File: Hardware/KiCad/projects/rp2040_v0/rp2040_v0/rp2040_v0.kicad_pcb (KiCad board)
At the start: 2 copper layers, 142 parts, among them J1 Conn_01x03, J11 Conn_01x02, J12 Screw_Terminal_01x02, J13 Conn_02x09_Counter_Clockwise, J14 Conn_02x06_Odd_Even, J15 Conn_01x02, J17 Conn_01x03, J18 Conn_01x03, J19 Conn_01x03, J2 Conn_01x02, J20 Conn_01x03, J21 Conn_01x03, J22 Conn_02x05_Odd_Even, J23 Screw_Terminal_01x02, J25 Screw_Terminal_01x02, J27 Screw_Terminal_01x02, J28 Screw_Terminal_01x02, J3 Conn_01x03, J4 Conn_01x04, J5 USB_B_Micro, J8 Conn_01x03, J9 Conn_01x02, Q1 2N7002, Q2 AO3400A, Q3 2N7002, Q4 AO3400A, Q5 AO3400A, U1 W25Q128JVSIQTR, U11 AMS1117-5.0, U12 DRV8837, U2 AMS1117-3.3, U3 RP2040, U4 AMS1117-5.0, U5 BMI088, U6 BMP280, U7 AMS1117-5.0, U8 AMS1117-5.0, U9 AMS1117-5.0, X1 X322512MSB4SI (12MHz)

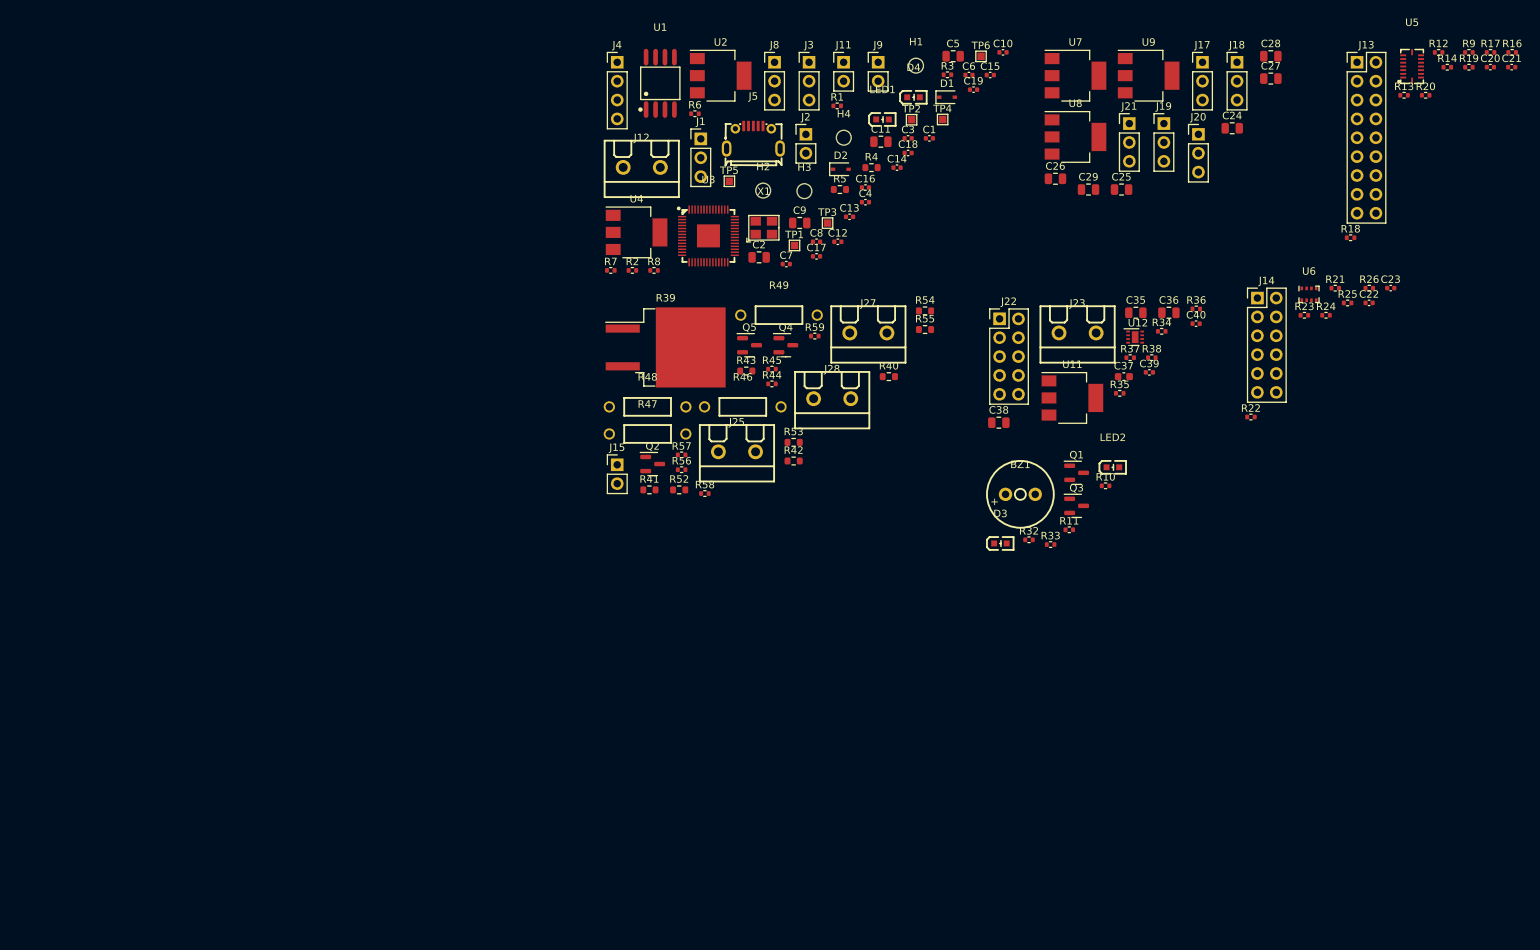
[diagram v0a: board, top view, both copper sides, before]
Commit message: Update leds and further layout work
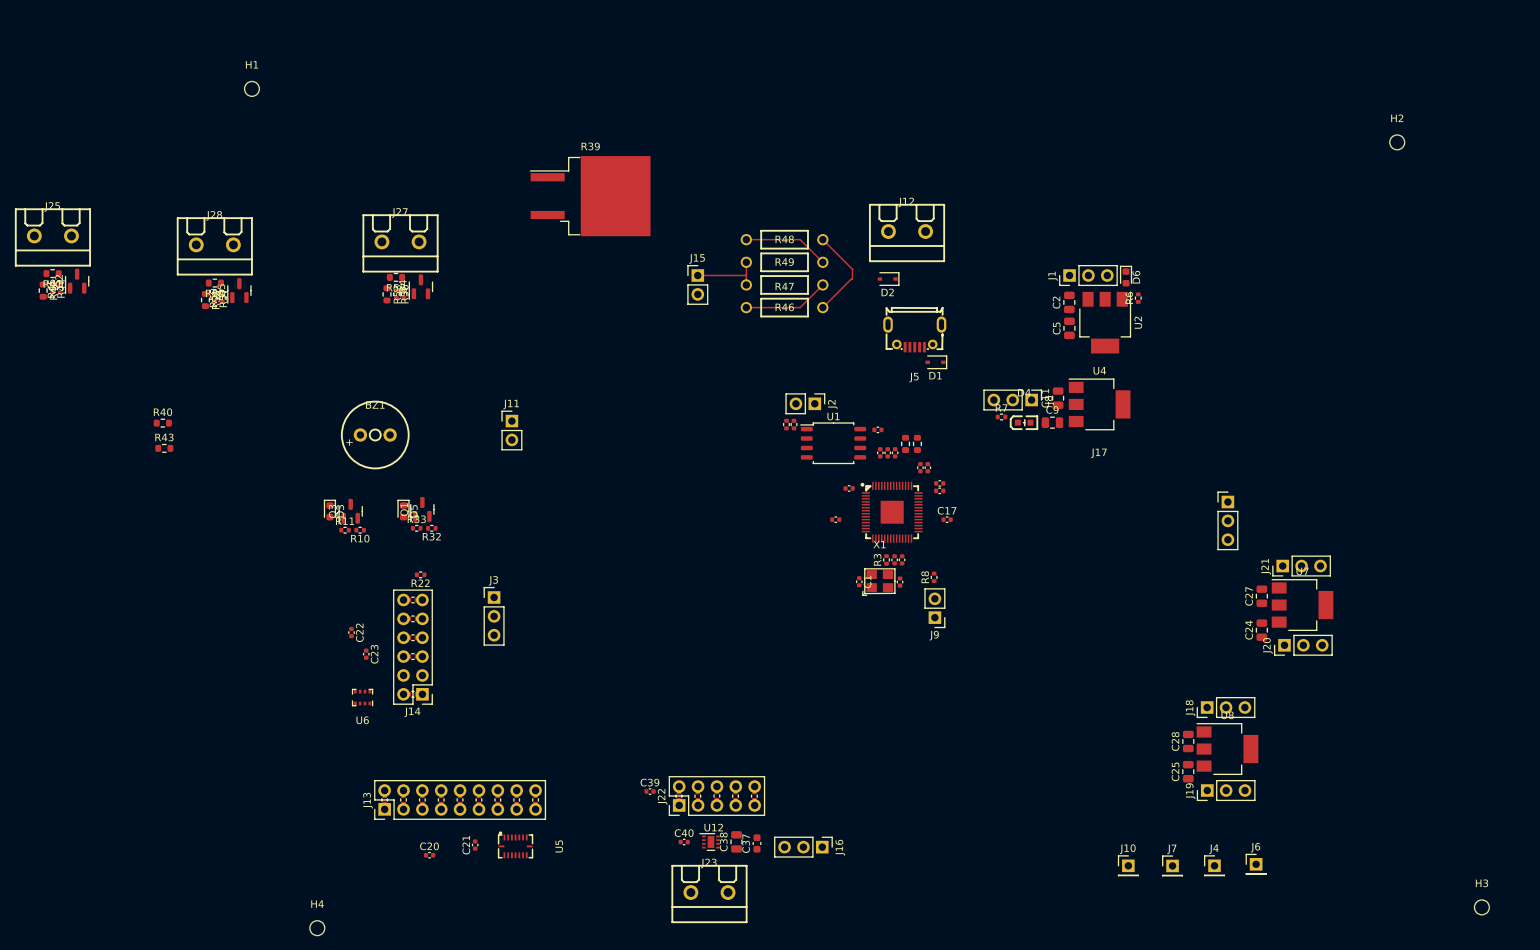
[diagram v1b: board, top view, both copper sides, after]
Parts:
- removed C26, C29, C35, C36: 10uF, Capacitor_SMD:C_0805_2012Metric
- removed LED1, LED2: KT-0603R, easyeda2kicad:LED0603-R-RD
- removed TP1, TP2, TP3, TP4, TP5, TP6: TestPoint, TestPoint:TestPoint_Pad_1.0x1.0mm
- removed U11, U9: AMS1117-5.0, Package_TO_SOT_SMD:SOT-223-3_TabPin2
- added D5: LED-KT-0603R, LED_SMD:LED_0603_1608Metric, F.Cu at (82.8, 100.1)
- added D6: LED-KT-0603R, LED_SMD:LED_0603_1608Metric, F.Cu at (180.1, 68.6)
- added J10: Conn_01x01, Connector_PinHeader_2.54mm:PinHeader_1x01_P2.54mm_Vertical, F.Cu at (180.4, 147.8)
- added J16: Conn_01x03, Connector_PinHeader_2.54mm:PinHeader_1x03_P2.54mm_Vertical, F.Cu at (139.2, 145.3)
- added J6: Conn_01x01, Connector_PinHeader_2.54mm:PinHeader_1x01_P2.54mm_Vertical, F.Cu at (197.6, 147.6)
- added J7: Conn_01x01, Connector_PinHeader_2.54mm:PinHeader_1x01_P2.54mm_Vertical, F.Cu at (186.3, 147.8)
- D3: footprint easyeda2kicad:LED0603-R-RD -> LED_SMD:LED_0603_1608Metric
- J13: value Conn_02x09_Counter_Clockwise -> Conn_02x09_Odd_Even
- J4: value Conn_01x04 -> Conn_01x01; footprint Connector_PinHeader_2.54mm:PinHeader_1x04_P2.54mm_Vertical -> Connector_PinHeader_2.54mm:PinHeader_1x01_P2.54mm_Vertical
- U1: footprint easyeda2kicad:SOIC-8_L5.3-W5.3-P1.27-LS8.0-BL -> Package_SO:SOIC-8_5.23x5.23mm_P1.27mm
- X1: value X322512MSB4SI (12MHz) -> X322512MSB4SI
- moved C20 177.9 mm to (86.3, 146.4)
- moved R9 177.3 mm to (80.3, 138.9), turned to 90 degrees
- moved C21 174.5 mm to (92.5, 145.0), turned to 90 degrees
- moved R16 173.8 mm to (90.4, 138.9), turned to 90 degrees
- moved R12 171.9 mm to (82.8, 138.9), turned to 90 degrees
- moved R17 169.4 mm to (93.0, 138.9), turned to 90 degrees
- moved R14 167.6 mm to (87.9, 138.9), turned to 90 degrees
- moved J13 165.1 mm to (80.3, 140.2), turned to 90 degrees
- moved R13 162.7 mm to (85.3, 138.9), turned to 90 degrees
- moved R19 161.8 mm to (98.0, 138.9), turned to 90 degrees
- moved U5 160.0 mm to (97.9, 145.2), turned to -90 degrees
- moved R20 152.9 mm to (100.6, 138.9), turned to 90 degrees
- moved C23 146.5 mm to (77.8, 119.3), turned to -90 degrees
- moved C22 144.0 mm to (75.8, 116.4), turned to -90 degrees
- moved U6 138.5 mm to (77.3, 125.2), turned to 180 degrees
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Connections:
- net 5v_MOTOR renamed MOTOR_POWER
- BZ1 pad 2: -BATT -> GND
- C1 pad 1: -BATT -> GND
- C10 pad 2: -BATT -> GND
- C11 pad 2: -BATT -> GND
- C12 pad 2: -BATT -> GND
- C13 pad 2: -BATT -> GND
- C14 pad 2: -BATT -> GND
- C15 pad 2: -BATT -> GND
- C16 pad 2: -BATT -> GND
- C17 pad 2: -BATT -> GND
- C18 pad 2: -BATT -> GND
- C19 pad 2: -BATT -> GND
- C2 pad 1: -BATT -> GND
- C20 pad 1: Net-(C21-Pad1) -> Net-(C20-Pad1)
- C20 pad 2: -BATT -> GND
- C21 pad 1: Net-(C21-Pad1) -> Net-(C20-Pad1)
- C21 pad 2: -BATT -> GND
- C22 pad 2: -BATT -> GND
- C23 pad 2: -BATT -> GND
- C24 pad 1: -BATT -> GND
- C25 pad 1: -BATT -> GND
- C27 pad 2: -BATT -> GND
- C28 pad 2: -BATT -> GND
- C3 pad 2: -BATT -> GND
- C37 pad 2: -BATT -> GND
- C38 pad 2: -BATT -> GND
- C39 pad 2: -BATT -> GND
- C4 pad 2: -BATT -> GND
- C40 pad 2: -BATT -> GND
- C5 pad 2: -BATT -> GND
- C6 pad 1: -BATT -> GND
- C7 pad 2: -BATT -> GND
- C8 pad 1: -BATT -> GND
- C9 pad 1: -BATT -> GND
- D4 pad 1: -BATT -> GND
- J12 pad 2: -BATT -> GND
- J13 pad 10: SPI0_SCK__BMI088_SCLK -> GYRO_INT
- J13 pad 11: SPI0_TX__BMI088_MOSI -> Net-(C20-Pad1)
- J13 pad 12: SPI0_RX__BMI088_MISO -> +3.3V
- J13 pad 13: +3.3V -> Net-(R18-Pad1)
- J13 pad 14: GYRO_INT -> SPI0_RX__BMI088_MISO
- J13 pad 15: SPI0_CSn__BMI088_CS_ACCEL -> Net-(R19-Pad1)
- J13 pad 16: SPI0_RX__BMI088_MISO -> SPI0_TX__BMI088_MOSI
- J13 pad 17: ACCEL_INT -> Net-(R20-Pad1)
- J13 pad 18: SPI0_CSn__BMI088_CS_GYRO -> SPI0_SCK__BMI088_SCLK
- J13 pad 2: Net-(R12-Pad1) -> SPI0_CSn__BMI088_CS_GYRO
- J13 pad 3: Net-(R13-Pad1) -> Net-(R12-Pad1)
- J13 pad 4: Net-(R14-Pad1) -> ACCEL_INT
- J13 pad 5: Net-(R16-Pad1) -> Net-(R13-Pad1)
- J13 pad 6: Net-(C21-Pad1) -> SPI0_RX__BMI088_MISO
- J13 pad 7: Net-(R18-Pad1) -> Net-(R14-Pad1)
- J13 pad 8: Net-(R19-Pad1) -> SPI0_CSn__BMI088_CS_ACCEL
- J13 pad 9: Net-(R20-Pad1) -> Net-(R16-Pad1)
- J17 pad 2: 5v_Servo_E -> +5V
- J17 pad 3: -BATT -> GND
- J18 pad 3: -BATT -> GND
- J19 pad 3: -BATT -> GND
- J2 pad 1: -BATT -> GND
- J20 pad 3: -BATT -> GND
- J21 pad 3: -BATT -> GND
- J3 pad 2: -BATT -> GND
- J4 pad 1: -BATT -> Protected_VBATT+
- J5 pad 5: -BATT -> GND
- J5 pad 6: -BATT -> GND
- J9 pad 1: -BATT -> GND
- Q1 pad 2: -BATT -> GND
- Q2 pad 2: -BATT -> GND
- Q3 pad 2: -BATT -> GND
- Q4 pad 2: -BATT -> GND
- Q5 pad 2: -BATT -> GND
- R17 pad 1: Net-(C21-Pad1) -> Net-(C20-Pad1)
- R40 pad 2: -BATT -> GND
- R42 pad 2: -BATT -> GND
- R44 pad 1: -BATT -> GND
- R53 pad 2: -BATT -> GND
- R55 pad 2: -BATT -> GND
- R56 pad 1: -BATT -> GND
- R57 pad 1: -BATT -> GND
- R6 pad 1: +5V -> +3.3V
- U1 pad 2: /QSPI_SD0 -> /QSPI_SD1
- U1 pad 4: -BATT -> GND
- U1 pad 5: /QSPI_SD1 -> /QSPI_SD0
- U12 pad 4: -BATT -> GND
- U12 pad 9: -BATT -> GND
- U2 pad 1: -BATT -> GND
- U3 pad 19: -BATT -> GND
- U3 pad 57: -BATT -> GND
- U4 pad 1: -BATT -> GND
- U5 pad 11: Net-(C21-Pad1) -> Net-(C20-Pad1)
- U5 pad 2: -BATT -> GND
- U5 pad 3: Net-(C21-Pad1) -> Net-(C20-Pad1)
- U5 pad 4: -BATT -> GND
- U5 pad 6: -BATT -> GND
- U5 pad 7: -BATT -> GND
- U6 pad 1: -BATT -> GND
- U6 pad 7: -BATT -> GND
- U7 pad 1: -BATT -> GND
- U8 pad 1: -BATT -> GND
- X1 pad 2: -BATT -> GND
- X1 pad 4: -BATT -> GND
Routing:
- net +BATT: track 0.00 -> 12.6 mm
- net Net-(R48-Pad2): track 0.00 -> 11.6 mm
- net Net-(R46-Pad2): track 0.00 -> 11.6 mm
- net Net-(J15-Pad1): track 0.00 -> 9.61 mm

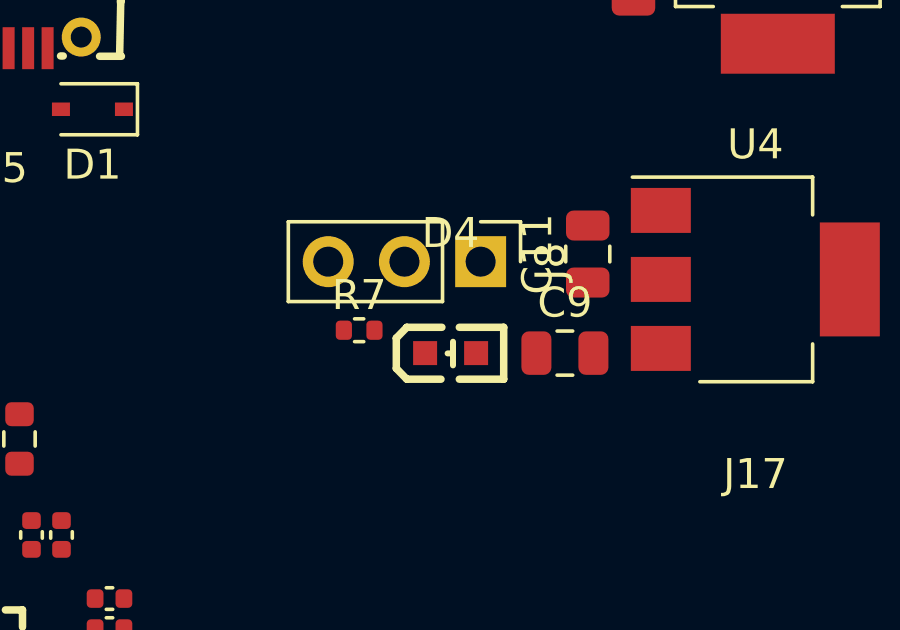
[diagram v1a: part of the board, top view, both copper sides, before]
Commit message: update pcb with new pinout
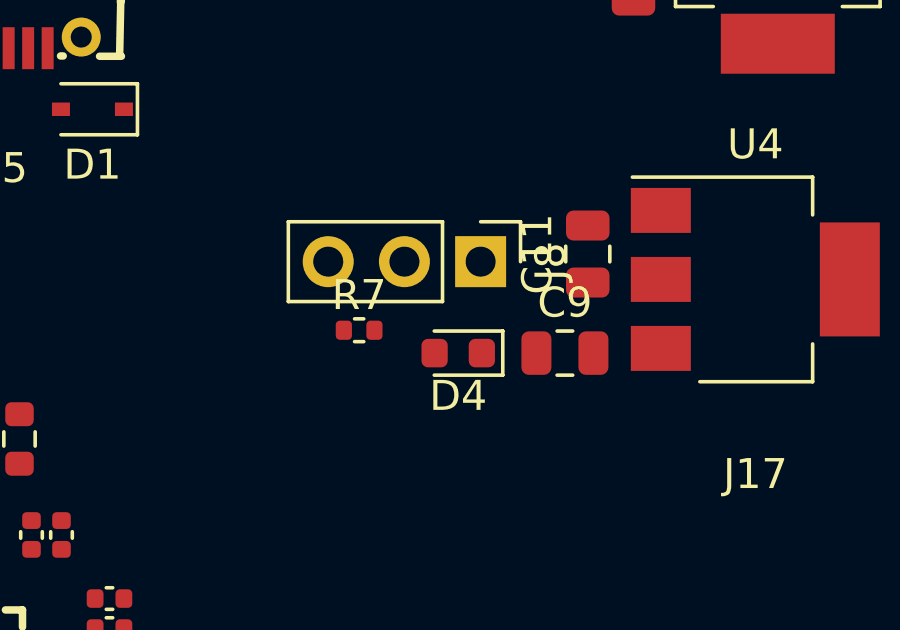
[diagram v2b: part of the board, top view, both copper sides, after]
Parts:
- D4: footprint easyeda2kicad:LED0603-R-RD -> LED_SMD:LED_0603_1608Metric
- moved D4 0.25 mm to (166.6, 88.1), turned to 180 degrees
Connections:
- U3 pad 16: Pyro_Control_A -> User_controlled_LED_A
- U3 pad 18: Pyro_Control_B -> User_controlled_LED_B
- U3 pad 28: Pyro_Control_C -> Pyro_Control_A
- U3 pad 30: User_controlled_LED_B -> Pyro_Control_B
- U3 pad 37: User_controlled_LED_A -> Pyro_Control_C

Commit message: ON NO! I didn't realize the IMU is not in the center of the board and it really ought to be. What to do what to do...
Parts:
- removed C10: 100nF, Capacitor_SMD:C_0402_1005Metric
- moved J25 129.6 mm to (143.3, 135.1), turned to 180 degrees
- moved R42 124.3 mm to (144.6, 127.8), turned to 90 degrees
- moved R41 124.3 mm to (143.3, 130.1), turned to 0 degrees
- moved R44 122.3 mm to (143.3, 128.0), turned to 90 degrees
- moved R45 120.5 mm to (142.3, 128.0), turned to -90 degrees
- moved Q2 117.6 mm to (140.0, 129.0), turned to -90 degrees
- moved H3 115.8 mm to (112.6, 143.0)
- moved J28 102.9 mm to (132.1, 135.0), turned to 180 degrees
- moved R43 101.3 mm to (147.4, 62.0), turned to 180 degrees
- moved J13 99.0 mm to (115.3, 47.6), turned to 0 degrees
- moved R9 98.3 mm to (116.6, 47.6), turned to 0 degrees
- moved R40 96.6 mm to (142.0, 57.4), turned to 90 degrees
- moved R54 96.2 mm to (132.1, 129.9), turned to 0 degrees
- moved R55 95.4 mm to (133.4, 127.6), turned to 90 degrees
- moved R12 95.0 mm to (116.6, 50.2), turned to 0 degrees
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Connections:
- net Net-(R4-Pad1) renamed /D+
- net Net-(R5-Pad2) renamed /D-
- J13 pad 11: Net-(C20-Pad1) -> Net-(J13-Pad11)
- J13 pad 12: +3.3V -> SPI0_CSn__BMI088_CS_ACCEL
- J13 pad 16: SPI0_TX__BMI088_MOSI -> ACCEL_INT
- J13 pad 18: SPI0_SCK__BMI088_SCLK -> SPI0_CSn__BMI088_CS_GYRO
- J13 pad 2: SPI0_CSn__BMI088_CS_GYRO -> SPI0_SCK__BMI088_SCLK
- J13 pad 4: ACCEL_INT -> SPI0_TX__BMI088_MOSI
- J13 pad 7: Net-(J13-Pad7) -> Net-(C20-Pad1)
- J13 pad 8: SPI0_CSn__BMI088_CS_ACCEL -> +3.3V
- J14 pad 11: SPI1_CSn__BMP280_CSn -> SPI1_RX__BMP280_MISO
- J14 pad 5: SPI1_SCK__BMP280_SCLK -> SPI1_TX__BMP280_MOSI
- J14 pad 7: SPI1_TX__BMP280_MOSI -> SPI1_SCK__BMP280_SCLK
- J14 pad 9: SPI1_RX__BMP280_MISO -> SPI1_CSn__BMP280_CSn
- J15 pad 1: Net-(J15-Pad1) -> +BATT
- J15 pad 2: Armed_Batt+_with_big_pyro_resistor -> Net-(J15-Pad2)
- J22 pad 1: MOTOR_POWER -> Net-(J22-Pad1)
- J22 pad 10: Net-(J22-Pad10) -> MOTOR_POWER
- J22 pad 2: Net-(C37-Pad1) -> PWM_6_A__Reaction_Control_Wheel_In_A
- J22 pad 3: +3.3V -> Net-(J22-Pad3)
- J22 pad 4: Net-(C40-Pad1) -> PWM_7_A__Reaction_Control_Wheel_In_B
- J22 pad 5: +3.3V -> Net-(J22-Pad5)
- J22 pad 6: Net-(J22-Pad6) -> +3.3V
- J22 pad 7: PWM_7_A__Reaction_Control_Wheel_In_B -> Net-(C40-Pad1)
- J22 pad 8: Net-(J22-Pad8) -> +3.3V
- J22 pad 9: PWM_6_A__Reaction_Control_Wheel_In_A -> Net-(C37-Pad1)
- R12 pad 2: ACCEL_INT -> SPI0_TX__BMI088_MOSI
- R14 pad 1: Net-(J13-Pad7) -> Net-(C20-Pad1)
- R14 pad 2: SPI0_CSn__BMI088_CS_ACCEL -> +3.3V
- R17 pad 1: Net-(C20-Pad1) -> Net-(J13-Pad11)
- R17 pad 2: +3.3V -> SPI0_CSn__BMI088_CS_ACCEL
- R19 pad 2: SPI0_TX__BMI088_MOSI -> ACCEL_INT
- R20 pad 2: SPI0_SCK__BMI088_SCLK -> SPI0_CSn__BMI088_CS_GYRO
- R23 pad 1: SPI1_SCK__BMP280_SCLK -> SPI1_TX__BMP280_MOSI
- R24 pad 1: SPI1_TX__BMP280_MOSI -> SPI1_SCK__BMP280_SCLK
- R25 pad 1: SPI1_RX__BMP280_MISO -> SPI1_CSn__BMP280_CSn
- R26 pad 1: SPI1_CSn__BMP280_CSn -> SPI1_RX__BMP280_MISO
- R34 pad 1: MOTOR_POWER -> Net-(J22-Pad1)
- R34 pad 2: Net-(C37-Pad1) -> PWM_6_A__Reaction_Control_Wheel_In_A
- R35 pad 1: +3.3V -> Net-(J22-Pad3)
- R35 pad 2: Net-(C40-Pad1) -> PWM_7_A__Reaction_Control_Wheel_In_B
- R36 pad 1: +3.3V -> Net-(J22-Pad5)
- R36 pad 2: Net-(J22-Pad6) -> +3.3V
- R37 pad 1: PWM_7_A__Reaction_Control_Wheel_In_B -> Net-(C40-Pad1)
- R37 pad 2: Net-(J22-Pad8) -> +3.3V
- R38 pad 1: PWM_6_A__Reaction_Control_Wheel_In_A -> Net-(C37-Pad1)
- R38 pad 2: Net-(J22-Pad10) -> MOTOR_POWER
- R39 pad 1: +BATT -> Net-(J15-Pad2)
- R39 pad 2: Net-(J15-Pad1) -> Armed_Batt+_with_big_pyro_resistor
- R46 pad 1: +BATT -> Net-(J15-Pad2)
- R47 pad 2: Net-(J15-Pad1) -> Armed_Batt+_with_big_pyro_resistor
- R48 pad 1: +BATT -> Net-(J15-Pad2)
- R49 pad 2: Net-(J15-Pad1) -> Armed_Batt+_with_big_pyro_resistor
- R9 pad 2: SPI0_CSn__BMI088_CS_GYRO -> SPI0_SCK__BMI088_SCLK
- U12 pad 5: Net-(J22-Pad10) -> Net-(J22-Pad1)
- U12 pad 6: Net-(J22-Pad8) -> Net-(J22-Pad3)
- U12 pad 7: Net-(J22-Pad6) -> Net-(J22-Pad5)
- U5 pad 10: Net-(J13-Pad13) -> Net-(J13-Pad5)
- U5 pad 14: Net-(J13-Pad7) -> Net-(J13-Pad11)
- U5 pad 15: Net-(J13-Pad5) -> Net-(J13-Pad13)
- U5 pad 16: Net-(J13-Pad3) -> Net-(J13-Pad15)
- U5 pad 5: Net-(J13-Pad1) -> Net-(J13-Pad17)
- U5 pad 8: Net-(J13-Pad17) -> Net-(J13-Pad1)
- U5 pad 9: Net-(J13-Pad15) -> Net-(J13-Pad3)
- U6 pad 2: Net-(J14-Pad12) -> Net-(J14-Pad10)
- U6 pad 3: Net-(J14-Pad8) -> Net-(J14-Pad6)
- U6 pad 4: Net-(J14-Pad6) -> Net-(J14-Pad8)
- U6 pad 5: Net-(J14-Pad10) -> Net-(J14-Pad12)
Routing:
- net +3.3V: track 0.00 -> 122.2 mm, vias 0 -> 6
- net GND: track 0.00 -> 74.0 mm, vias 0 -> 42
- net User_controlled_LED_B: track 0.00 -> 39.8 mm
- net User_controlled_LED_A: track 0.00 -> 37.2 mm
- net Buzzer: track 0.00 -> 34.6 mm, vias 0 -> 2
- net Net-(J13-Pad1): track 0.00 -> 30.2 mm
- net SPI0_RX__BMI088_MISO: track 0.00 -> 26.6 mm, vias 0 -> 2
- net Net-(J13-Pad3): track 0.00 -> 25.8 mm
- net Net-(J13-Pad5): track 0.00 -> 25.4 mm
- net Net-(C20-Pad1): track 0.00 -> 24.3 mm
- net SPI0_SCK__BMI088_SCLK: track 0.00 -> 20.6 mm
- net +1V1: track 0.00 -> 20.4 mm, vias 0 -> 4
- net SPI0_CSn__BMI088_CS_GYRO: track 0.00 -> 20.1 mm
- net Net-(J13-Pad9): track 0.00 -> 20.1 mm
- net SPI0_TX__BMI088_MOSI: track 0.00 -> 18.5 mm
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- added copper zone on F.Cu, net +1V1
- added copper zone on F.Cu, net +3.3V
- added copper zone on B.Cu, net GND
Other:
- board outline added: 99.6 x 101.6 mm
